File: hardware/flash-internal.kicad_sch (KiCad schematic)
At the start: 21 parts, among them J3 debug-flash, U3 74LVC8T245, U4 74LVC8T245, U5 74LVC8T245, U6 S29AL016J55TFIR20, U7 74LVC8T245, U8 74LVC8T245

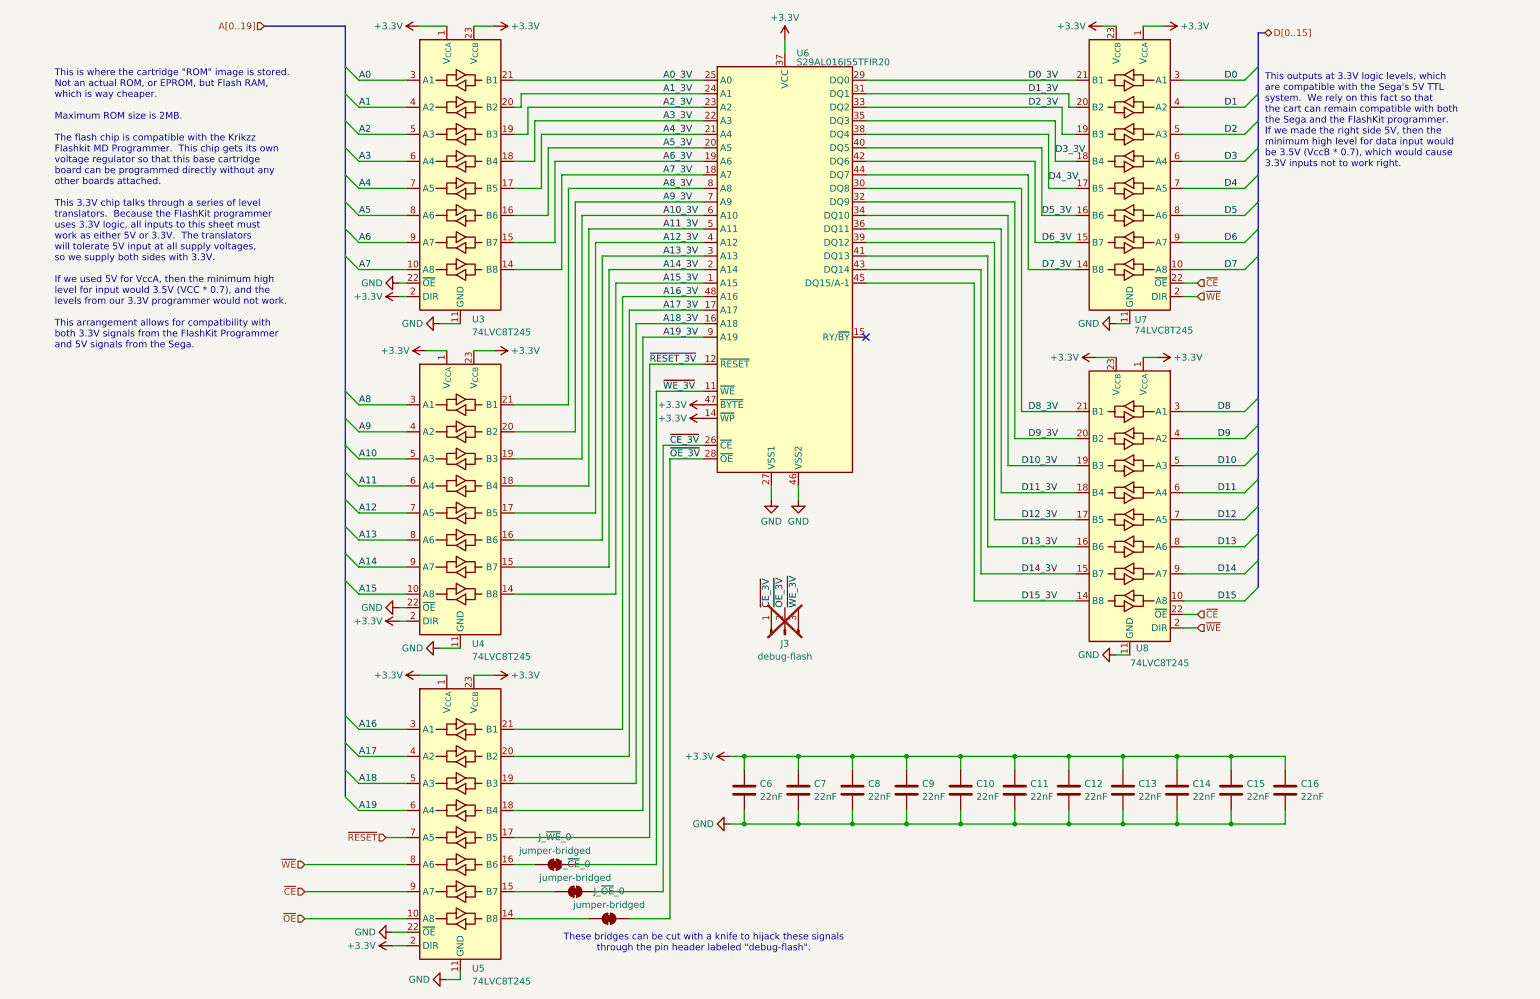
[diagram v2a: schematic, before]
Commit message: Fix cartridge board mistakes from v0.0.2
After getting the v0.0.2 cart board assembled, I found and fixed
several issues:
 - Fix address decoder output (Y0, not Y7)
 - Fix level-shifter direction for data (was backwards before)
 - Fix debug pad access to signals (level-shifters should use the
   internal signal, not the external one)
 - Avoid traces too close to the debug pads, since they can be cut
   accidentally

Also:
 - Add additional debug pad for both raw and level-shifted signals
 - Add debug pad and pin header for measuring current consumption
 - Replace bulk capacitor with SMD version
 - Remove pin headers that I didn't find all that useful in the last
   revision
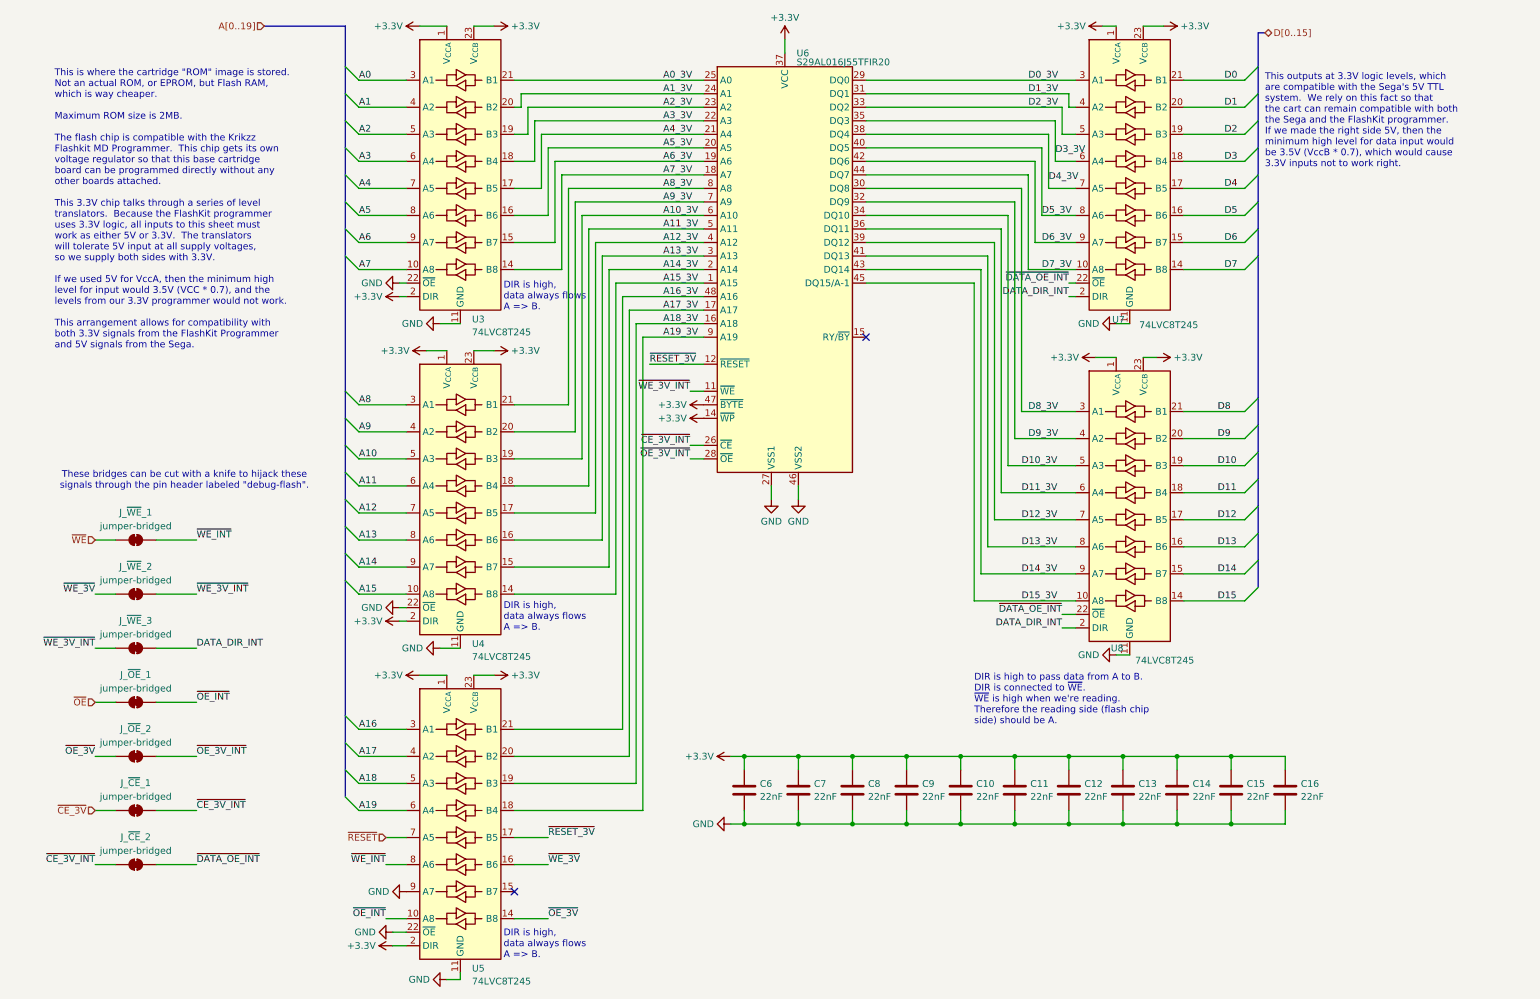
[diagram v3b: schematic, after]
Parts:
- removed J3: debug-flash, Connector_PinHeader_2.54mm:PinHeader_1x03_P2.54mm_Horizontal, symbol Connector:Conn_01x03_Pin
- removed J_~{CE}_0, J_~{OE}_0, J_~{WE}_0: jumper-bridged, Jumper:SolderJumper-2_P1.3mm_Bridged_RoundedPad1.0x1.5mm, symbol Jumper:SolderJumper_2_Bridged
- added J_~{CE}_1, J_~{CE}_2, J_~{OE}_1, J_~{OE}_2, J_~{WE}_1, J_~{WE}_2, J_~{WE}_3: jumper-bridged, Jumper:SolderJumper-2_P1.3mm_Bridged_RoundedPad1.0x1.5mm, symbol Jumper:SolderJumper_2_Bridged
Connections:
- net D0: now also U7.21 (B1); no longer U7.3 (A1)
- net D0_3V: now also U7.3 (A1); no longer U7.21 (B1)
- net D1: now also U7.20 (B2); no longer U7.4 (A2)
- net D10: now also U8.19 (B3); no longer U8.5 (A3)
- net D10_3V: now also U8.5 (A3); no longer U8.19 (B3)
- net D11: now also U8.18 (B4); no longer U8.6 (A4)
- net D11_3V: now also U8.6 (A4); no longer U8.18 (B4)
- net D12: now also U8.17 (B5); no longer U8.7 (A5)
- net D12_3V: now also U8.7 (A5); no longer U8.17 (B5)
- net D13: now also U8.16 (B6); no longer U8.8 (A6)
- net D13_3V: now also U8.8 (A6); no longer U8.16 (B6)
- net D14: now also U8.15 (B7); no longer U8.9 (A7)
- net D14_3V: now also U8.9 (A7); no longer U8.15 (B7)
- net D15: now also U8.14 (B8); no longer U8.10 (A8)
- net D15_3V: now also U8.10 (A8); no longer U8.14 (B8)
- net D1_3V: now also U7.4 (A2); no longer U7.20 (B2)
- net D2: now also U7.19 (B3); no longer U7.5 (A3)
- net D2_3V: now also U7.5 (A3); no longer U7.19 (B3)
- net D3: now also U7.18 (B4); no longer U7.6 (A4)
- net D3_3V: now also U7.6 (A4); no longer U7.18 (B4)
- net D4: now also U7.17 (B5); no longer U7.7 (A5)
- net D4_3V: now also U7.7 (A5); no longer U7.17 (B5)
- net D5: now also U7.16 (B6); no longer U7.8 (A6)
- net D5_3V: now also U7.8 (A6); no longer U7.16 (B6)
- net D6: now also U7.15 (B7); no longer U7.9 (A7)
- net D6_3V: now also U7.9 (A7); no longer U7.15 (B7)
- net D7: now also U7.14 (B8); no longer U7.10 (A8)
- net D7_3V: now also U7.10 (A8); no longer U7.14 (B8)
- net D8: now also U8.21 (B1); no longer U8.3 (A1)
- net D8_3V: now also U8.3 (A1); no longer U8.21 (B1)
- net D9: now also U8.20 (B2); no longer U8.4 (A2)
- net D9_3V: now also U8.4 (A2); no longer U8.20 (B2)
- net GND: now also U5.9 (A7)
- net ~{CE_3V}: now also J_~{CE}_1.1 (A); no longer U6.26 (~{CE})
- net ~{OE_3V}: now also U5.14 (B8), J_~{OE}_2.1 (A); no longer U6.28 (~{OE})
- net ~{OE}: now also J_~{OE}_1.1 (A); no longer U5.10 (A8)
- net ~{WE_3V}: now also U5.16 (B6), J_~{WE}_2.1 (A); no longer U6.11 (~{WE})
- net ~{WE}: now also J_~{WE}_1.1 (A); no longer U5.8 (A6), U7.2 (DIR), U8.2 (DIR)
- net ~{CE} renamed ~{DATA_OE_INT}
- net ~{DATA_OE_INT}: now also J_~{CE}_2.2 (B); no longer U5.9 (A7)
- new net DATA_DIR_INT: J_~{WE}_3.2 (B), U7.2 (DIR), U8.2 (DIR)
- new net ~{CE_3V_INT}: J_~{CE}_1.2 (B), J_~{CE}_2.1 (A), U6.26 (~{CE})
- new net ~{OE_3V_INT}: J_~{OE}_2.2 (B), U6.28 (~{OE})
- new net ~{OE_INT}: J_~{OE}_1.2 (B), U5.10 (A8)
- new net ~{WE_3V_INT}: J_~{WE}_2.2 (B), J_~{WE}_3.1 (A), U6.11 (~{WE})
- new net ~{WE_INT}: J_~{WE}_1.2 (B), U5.8 (A6)
- no-connect marks 1 -> 2
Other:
- note added: "DIR is high to pass data from A to B. DIR is connected to ~{WE}. ~{WE} is high when we're reading. Therefore the reading side (flash chip side) should be A."
- note added: "DIR is high, data always flows A => B."

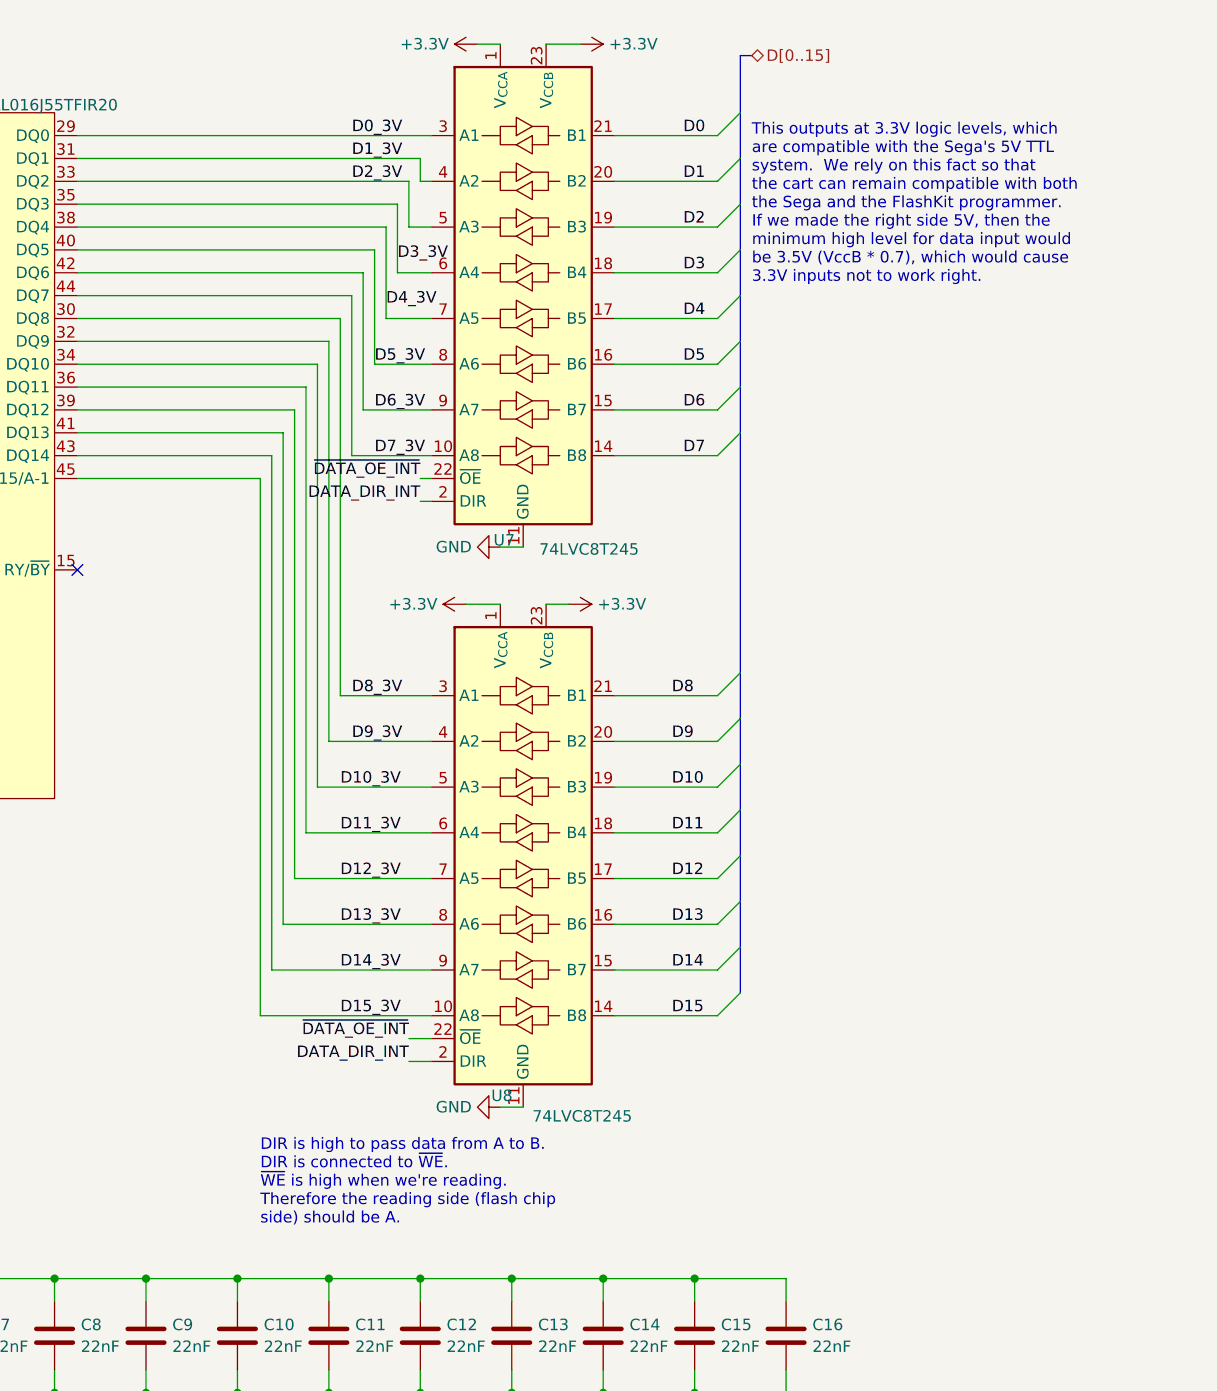
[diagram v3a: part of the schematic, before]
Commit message: Expand comments in flash schematic
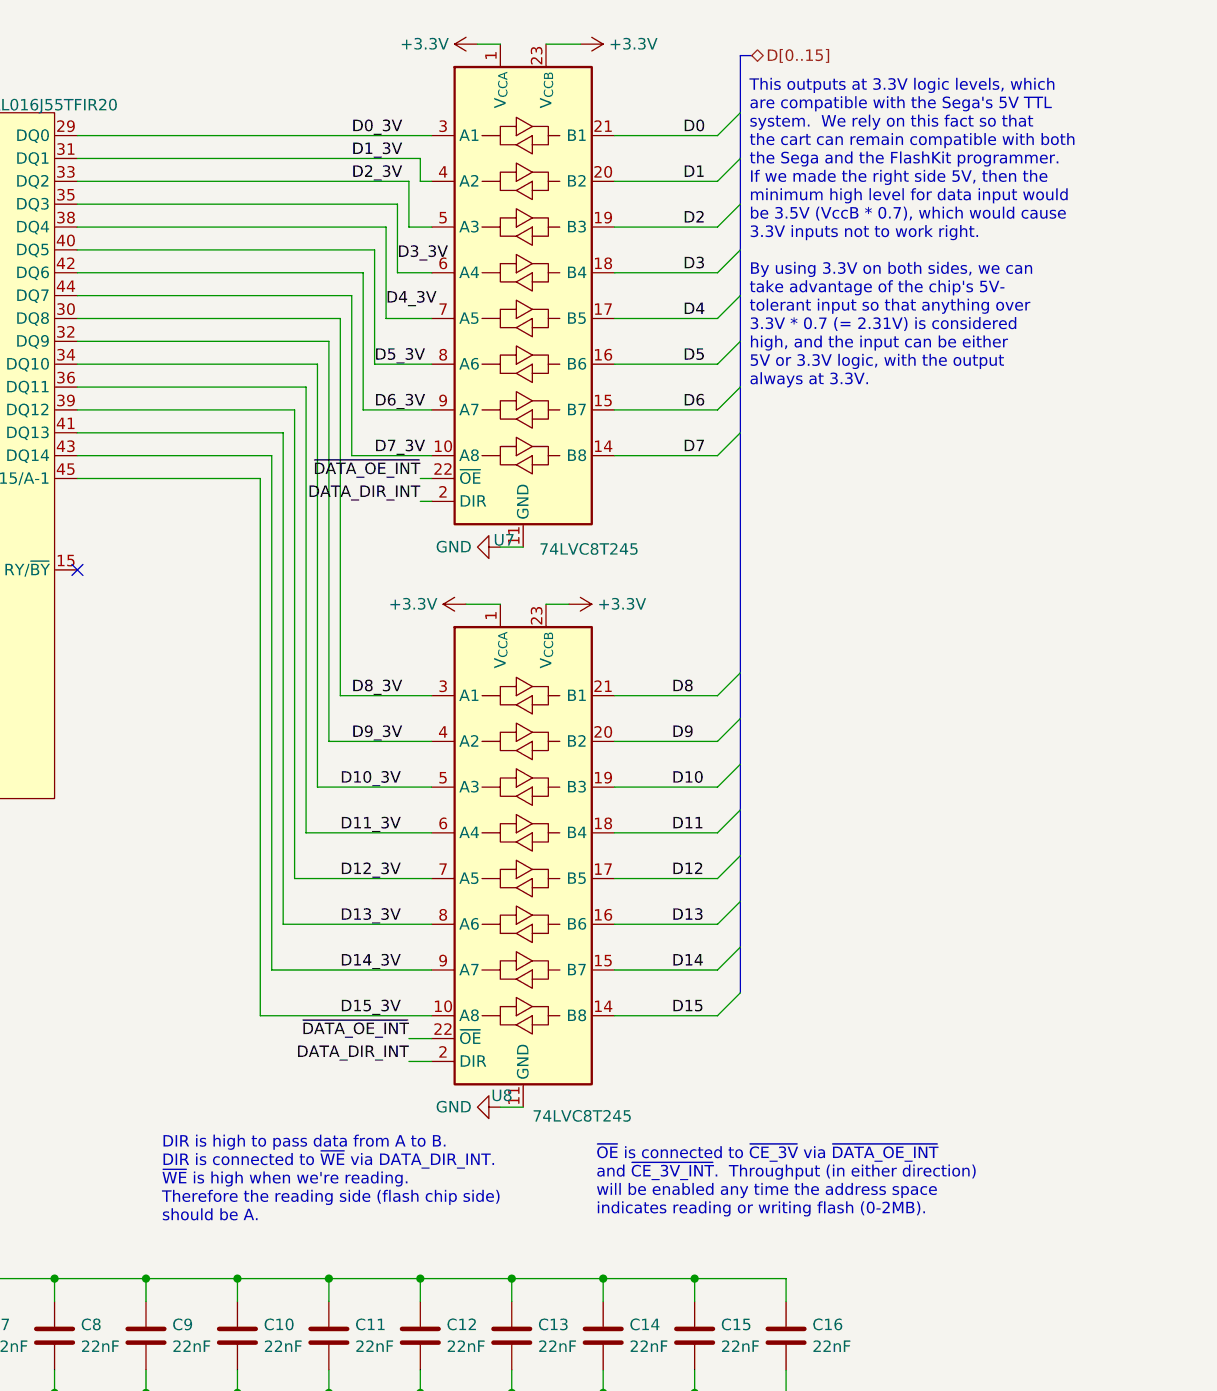
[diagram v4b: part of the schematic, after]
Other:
- note added: "DIR is high to pass data from A to B. DIR is connected to ~{WE} via DATA_DIR_INT. ~{WE} is high when we're reading. Therefore the reading side (flash chip side) should be A."
- note added: "This outputs at 3.3V logic levels, which are compatible with the Sega's 5V TTL system. We rely on this fact so that the cart can remain compatible with both the Sega and the FlashKit programmer. If we made the right side 5V, then the minimum high level for data input would be 3.5V (VccB * 0.7), which would cause 3.3V inputs not to work right. By using 3.3V on both sides, we can take advantage of 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"
- note added: "~{OE} is connected to ~{CE_3V} via ~{DATA_OE_INT} and ~{CE_3V_INT}. Throughput (in either direction) will be enabled any time the address space indicates reading or writing flash (0-2MB)."
- note removed: "DIR is high to pass data from A to B. DIR is connected to ~{WE}. ~{WE} is high when we're reading. Therefore the reading side (flash chip side) should be A."
- note removed: "This outputs at 3.3V logic levels, which are compatible with the Sega's 5V TTL system. We rely on this fact so that the cart can remain compatible with both the Sega and the FlashKit programmer. If we made the right side 5V, then the minimum high level for data input would be 3.5V (VccB * 0.7), which would cause 3.3V inputs not to work right."
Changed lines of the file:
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@@
 		)
 	)
-	(text "This outputs at 3.3V logic levels, which\nare compatible with the Sega's 5V TTL\nsystem.  We rely on this fact so that\nthe cart can remain compatible with both\nthe Sega and the FlashKit programmer.\nIf we made the right side 5V, then the\nminimum high level for data input would\nbe 3.5V (VccB * 0.7), which would cause\n3.3V inputs not to work right."
+	(text "This outputs at 3.3V logic levels, which\nare compatible with the Sega's 5V TTL\nsystem.  We rely on this fact so that\nthe cart can remain compatible with both\nthe Sega and the FlashKit programmer.\nIf we made the right side 5V, then the\nminimum high level for data input would\nbe 3.5V (VccB * 0.7), which would cause\n3.3V inputs not to work right.\n\nBy using 3.3V on both sides, we can\ntake advantage of the chip's 5V-\ntolerant input so that anything over\n3.3V * 0.7 (= 2.31V) is considered\nhigh, and the input can be either\n5V or 3.3V logic, with the output\nalways at 3.3V."
 		(exclude_from_sim no)
-		(at 243.84 33.02 0)
+		(at 243.586 36.322 0)
+		(effects
+			(font
+				(size 1.27 1.27)
+			)
+			(justify left)
+		)
+	)
+	(text "~{OE} is connected to ~{CE_3V} via ~{DATA_OE_INT}\nand ~{CE_3V_INT}.  Throughput (in either direction)\nwill be enabled any time the address space\nindicates reading or writing flash (0-2MB)."
+		(exclude_from_sim no)
+		(at 226.568 141.732 0)
 		(effects
 			(font
@@
 		)
 	)
-	(text "DIR is high to pass data from A to B.\nDIR is connected to ~{WE}.\n~{WE} is high when we're reading.\nTherefore the reading side (flash chip\nside) should be A."
+	(text "DIR is high to pass data from A to B.\nDIR is connected to ~{WE} via DATA_DIR_INT.\n~{WE} is high when we're reading.\nTherefore the reading side (flash chip side)\nshould be A."
 		(exclude_from_sim no)
-		(at 189.23 141.732 0)
+		(at 178.308 141.478 0)
 		(effects
 			(font
